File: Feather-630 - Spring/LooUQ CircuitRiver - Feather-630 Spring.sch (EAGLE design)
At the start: 25 parts, among them J1 FEATHERHOST-S, J2 FEATHERHOST-L, J3 CR-SPRING_HEADER, J4 JST_PH-2_T/H, J5 JST_PH-2_T/H, J6 QWIIC_VERTICAL, J7 CR-RAPIDSIO_VERTICAL, J8 DNF, P1 DNF, P2 DNF, P3 DNF, U2 LM2674_BUCK

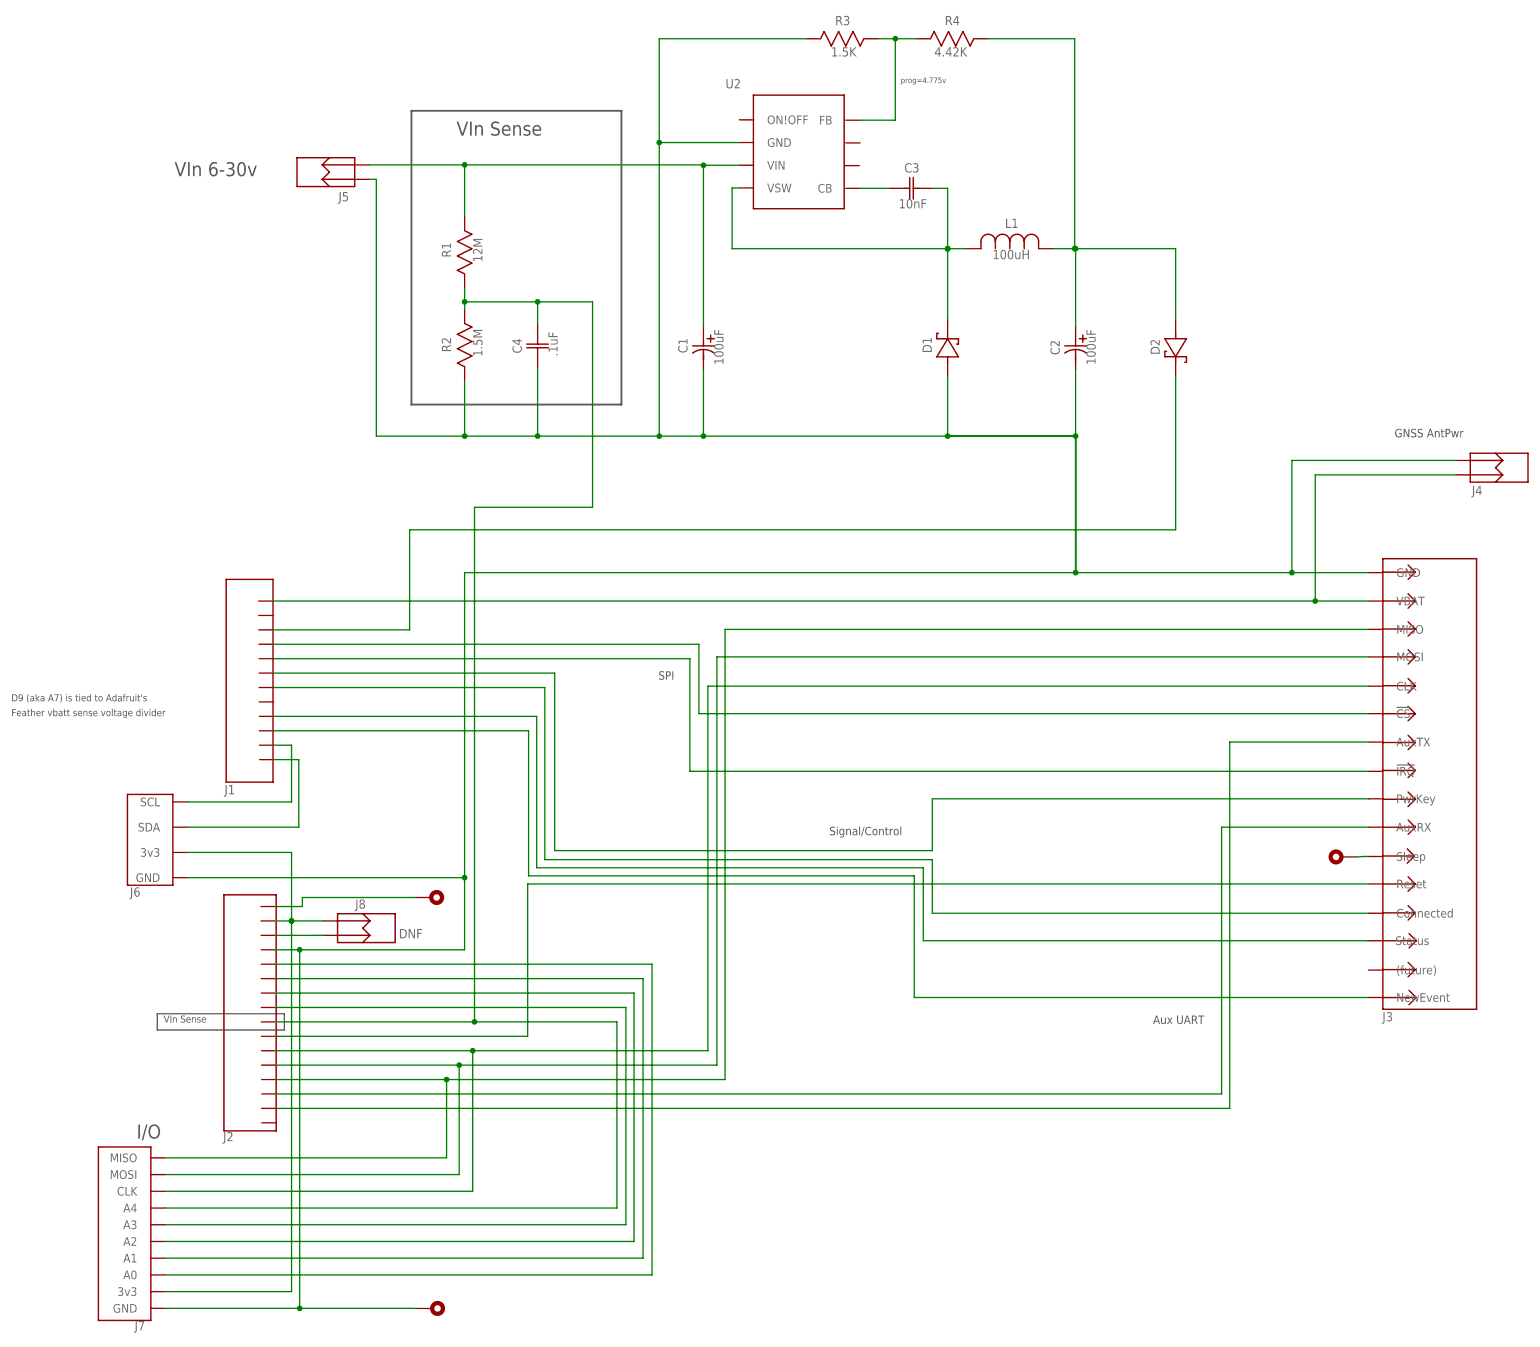
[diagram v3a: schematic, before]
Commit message: Moved RapidsIO, chg L1 on F-630
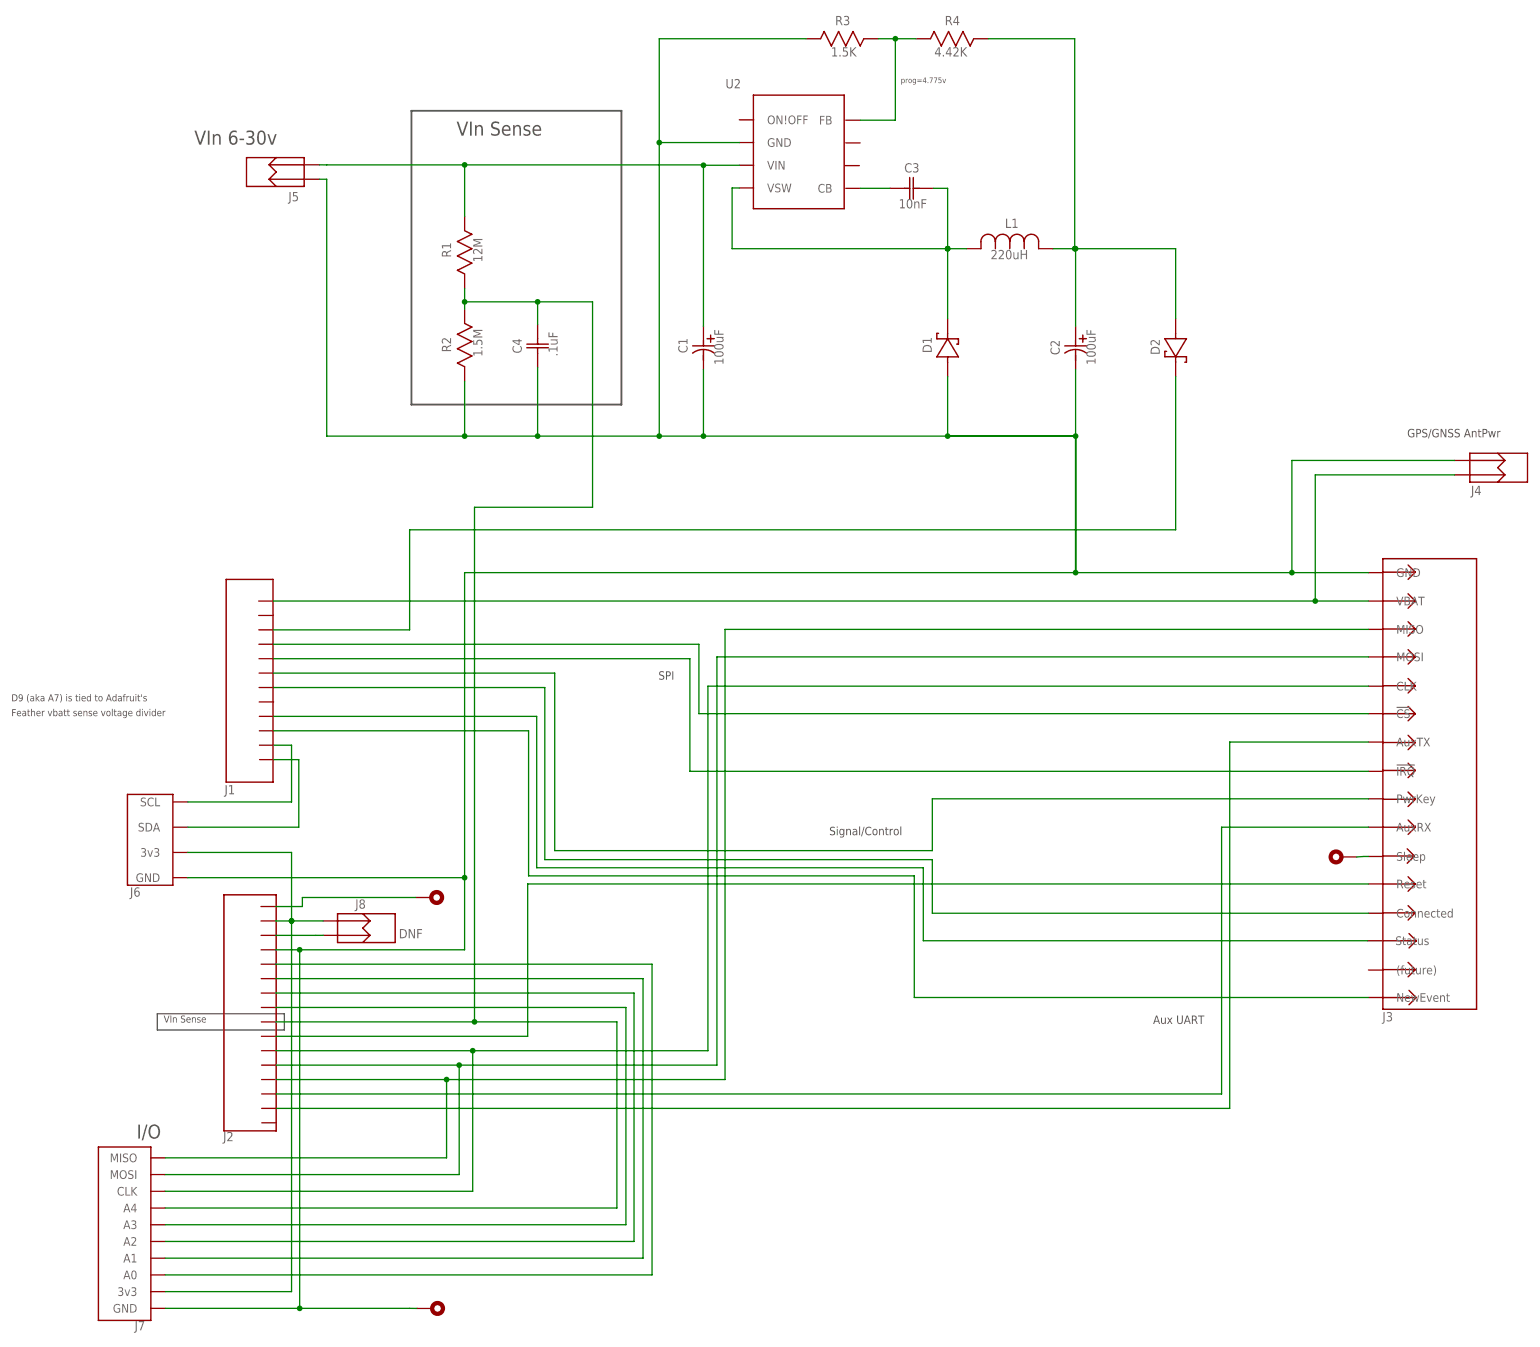
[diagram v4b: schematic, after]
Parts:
- J4: value JST_PH-2_T/H -> JST_PH-2_R/A_T/H; device common:JST_PH-2_T/H -> common:JST_PH-2_R/A_T/H
- J5: value JST_PH-2_T/H -> JST_PH-2_VERT_T/H; device common:JST_PH-2_T/H -> common:JST_PH-2_VERT_T/H
- L1: value 100uH -> 220uH; device common:SHIELDED_INDUCTOR_-_PANASONICH -> common:INDUCTOR_-_BOURNS_SRR1260
- LG1: value LOOUQ_LOGO -> DNF
- LG2: value CIRCUITRIVER_LOGO -> DNF
- P1, P2, P3: device common:DNF -> common:BREAKOUTPAD
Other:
- note added: "GPS/GNSS AntPwr"
- note removed: "GNSS AntPwr"
- moved on the sheet: J4, J5
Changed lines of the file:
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@@
 <part name="J2" library="common" deviceset="FEATHERHOST-L" device=""/>
 <part name="J3" library="common" deviceset="CR-SPRING_HEADER" device=""/>
-<part name="J4" library="common" deviceset="JST_PH-2_T/H" device=""/>
-<part name="J5" library="common" deviceset="JST_PH-2_T/H" device=""/>
+<part name="J4" library="common" deviceset="JST_PH-2_R/A_T/H" device=""/>
+<part name="J5" library="common" deviceset="JST_PH-2_VERT_T/H" device=""/>
 <part name="J6" library="common" deviceset="QWIIC_VERTICAL" device=""/>
 <part name="J7" library="common" deviceset="CR-RAPIDSIO_VERTICAL" device=""/>
 <part name="J8" library="common" deviceset="2PIN_T/H_HEADER" device="" value="DNF"/>
-<part name="L1" library="common" deviceset="SHIELDED_INDUCTOR_-_PANASONICH" device="" value="100uH"/>
-<part name="LG1" library="common" deviceset="LOOUQ_LOGO" device=""/>
-<part name="LG2" library="common" deviceset="CIRCUITRIVER_LOGO" device=""/>
-<part name="P1" library="common" deviceset="DNF" device=""/>
-<part name="P2" library="common" deviceset="DNF" device=""/>
-<part name="P3" library="common" deviceset="DNF" device=""/>
+<part name="L1" library="common" deviceset="INDUCTOR_-_BOURNS_SRR1260" device="" value="220uH"/>
+<part name="LG1" library="common" deviceset="LOOUQ_LOGO" device="" value="DNF"/>
+<part name="LG2" library="common" deviceset="CIRCUITRIVER_LOGO" device="" value="DNF"/>
+<part name="P1" library="common" deviceset="BREAKOUTPAD" device="" value="DNF"/>
+<part name="P2" library="common" deviceset="BREAKOUTPAD" device="" value="DNF"/>
+<part name="P3" library="common" deviceset="BREAKOUTPAD" device="" value="DNF"/>
 <part name="R1" library="common" deviceset="RES_0603" device="" value="12M"/>
 <part name="R2" library="common" deviceset="RES_0603" device="" value="1.5M"/>
@@
 <sheet>
 <plain>
-<text x="-103.334" y="116.351" size="2.467" layer="97" font="vector" ratio="10" rot="R0" align="top-left" distance="50">VIn 6-30v</text>
-<text x="111.59" y="69.366" size="1.48" layer="97" font="vector" ratio="10" rot="R0" align="top-left" distance="50">GNSS AntPwr</text>
+<text x="-99.842" y="121.908" size="2.467" layer="97" font="vector" ratio="10" rot="R0" align="top-left" distance="50">VIn 6-30v</text>
+<text x="113.812" y="69.366" size="1.48" layer="97" font="vector" ratio="10" rot="R0" align="top-left" distance="50">GPS/GNSS AntPwr</text>
 <text x="-132.069" y="22.616" size="1.233" layer="97" font="vector" ratio="10" rot="R0" align="top-left" distance="50">D9 (aka A7) is tied to Adafruit's</text>
 <text x="-53.651" y="123.495" size="2.467" layer="97" font="vector" ratio="10" rot="R0" align="top-left" distance="50">VIn Sense</text>
@@
 <attribute name="NAME" value="J3" layer="95" x="109.448" y="-33.368" size="1.628" align="top-left"/>
 </instance>
-<instance part="J4" gate="PART_1" x="130.004" y="62.541" rot="R180">
-<attribute name="NAME" value="J4" layer="95" x="125.206" y="59.34" size="1.628" align="top-left"/>
-</instance>
-<instance part="J5" gate="PART_1" x="-76.669" y="114.605">
-<attribute name="NAME" value="J5" layer="95" x="-74.446" y="111.087" size="1.628" align="top-left"/>
+<instance part="J4" gate="PART_1" x="129.845" y="62.541">
+<attribute name="NAME" value="J4" layer="95" x="125.047" y="59.34" size="1.628" align="top-left"/>
+</instance>
+<instance part="J5" gate="PART_1" x="-85.487" y="114.617" rot="R180">
+<attribute name="NAME" value="J5" layer="95" x="-83.264" y="111.099" size="1.628" align="top-left"/>
 </instance>
 <instance part="J6" gate="PART_1" x="-107.56" y="-3.016" rot="R90">
@@
 <instance part="L1" gate="PART_1" x="43.809" y="102.383">
 <attribute name="NAME" value="L1" layer="95" x="42.954" y="106.397" size="1.628" align="top-left"/>
-<attribute name="VALUE" value="100uH" layer="96" x="40.753" y="100.883" size="1.628" align="top-left"/>
+<attribute name="VALUE" value="220uH" layer="96" x="40.426" y="100.883" size="1.628" align="top-left"/>
 </instance>
 <instance part="LG1" gate="PART_1" x="114.776" y="131.128"/>
-<instance part="LG2" gate="PART_1" x="115.24" y="125.093"/>
+<instance part="LG2" gate="PART_1" x="114.617" y="124.46"/>
 <instance part="P1" gate="BRKOUTPAD" x="-57.229" y="-13.176" rot="R90"/>
 <instance part="P2" gate="BRKOUTPAD" x="-57.071" y="-85.566" rot="R90"/>
@@
 <wire layer="91" width="0.25" x1="55.401" y1="44.05" x2="55.401" y2="68.097"/>
 <wire layer="91" width="0.25" x1="55.401" y1="79.851" x2="55.401" y2="44.05"/>
-<wire layer="91" width="0.25" x1="-52.223" y1="68.097" x2="-67.779" y2="68.097"/>
+<wire layer="91" width="0.25" x1="-52.223" y1="68.097" x2="-76.518" y2="68.097"/>
 <wire layer="91" width="0.25" x1="-39.366" y1="68.097" x2="-52.223" y2="68.097"/>
 <wire layer="91" width="0.25" x1="-17.937" y1="68.097" x2="-39.366" y2="68.097"/>
@@
 <wire layer="91" width="0.25" x1="32.861" y1="68.097" x2="55.401" y2="68.097"/>
 <wire layer="91" width="0.25" x1="55.401" y1="68.097" x2="-10.155" y2="68.097"/>
-<wire layer="91" width="0.25" x1="-67.779" y1="113.335" x2="-69.049" y2="113.335"/>
-<wire layer="91" width="0.25" x1="-67.779" y1="68.097" x2="-67.779" y2="113.335"/>
+<wire layer="91" width="0.25" x1="-76.518" y1="113.347" x2="-77.788" y2="113.347"/>
+<wire layer="91" width="0.25" x1="-76.518" y1="68.097" x2="-76.518" y2="113.347"/>
 <pinref part="C2" gate="PART_1" pin="MINUS"/>
 <pinref part="J5" gate="PART_1" pin="P2"/>
@@
 <pinref part="J2" gate="PART_1" pin="GND@2"/>
 <pinref part="J3" gate="PART_1" pin="GND"/>
-<wire layer="91" width="0.25" x1="122.384" y1="63.811" x2="93.504" y2="63.811"/>
+<wire layer="91" width="0.25" x1="122.145" y1="63.811" x2="93.504" y2="63.811"/>
 <wire layer="91" width="0.25" x1="93.504" y1="63.811" x2="93.504" y2="44.05"/>
 <pinref part="J4" gate="PART_1" pin="P2"/>
@@
 <pinref part="J7" gate="PART_1" pin="GND"/>
 <junction x="-81.28" y="-22.388"/>
-<wire layer="91" width="0.25" x1="-61.912" y1="-85.551" x2="-60.643" y2="-85.566"/>
+<wire layer="91" width="0.25" x1="-61.912" y1="-85.551" x2="-60.642" y2="-85.566"/>
 <wire layer="91" width="0.25" x1="-61.912" y1="-85.551" x2="-81.28" y2="-85.551"/>
 <pinref part="P2" gate="BRKOUTPAD" pin="1"/>
@@
 <pinref part="J1" gate="PART_1" pin="VBAT"/>
 <pinref part="J3" gate="PART_1" pin="VBAT"/>
-<wire layer="91" width="0.25" x1="122.384" y1="61.271" x2="97.621" y2="61.271"/>
+<wire layer="91" width="0.25" x1="122.145" y1="61.271" x2="97.621" y2="61.271"/>
 <wire layer="91" width="0.25" x1="97.621" y1="61.271" x2="97.621" y2="39.048"/>
 <pinref part="J4" gate="PART_1" pin="P1"/>
@@
 <pinref part="U2" gate="PART_1" pin="VIN"/>
 <junction x="-10.155" y="115.81"/>
-<wire layer="91" width="0.25" x1="-52.223" y1="115.875" x2="-69.049" y2="115.875"/>
+<wire layer="91" width="0.25" x1="-76.518" y1="115.875" x2="-77.788" y2="115.887"/>
+<wire layer="91" width="0.25" x1="-52.223" y1="115.875" x2="-76.518" y2="115.875"/>
 <pinref part="J5" gate="PART_1" pin="P1"/>
 <junction x="-52.223" y="115.875"/>
